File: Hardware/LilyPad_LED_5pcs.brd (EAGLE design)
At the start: 27.4 x 12.8 mm, 27 parts

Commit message: Updated Brd File
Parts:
- moved U$3 0.22 mm to (14.0, 6.61)
- moved U$5 0.20 mm to (25.1, 6.63)
- moved U$1 0.20 mm to (2.75, 6.62)
- moved U$4 0.20 mm to (19.5, 6.60)
- moved U$2 0.18 mm to (8.38, 6.61)

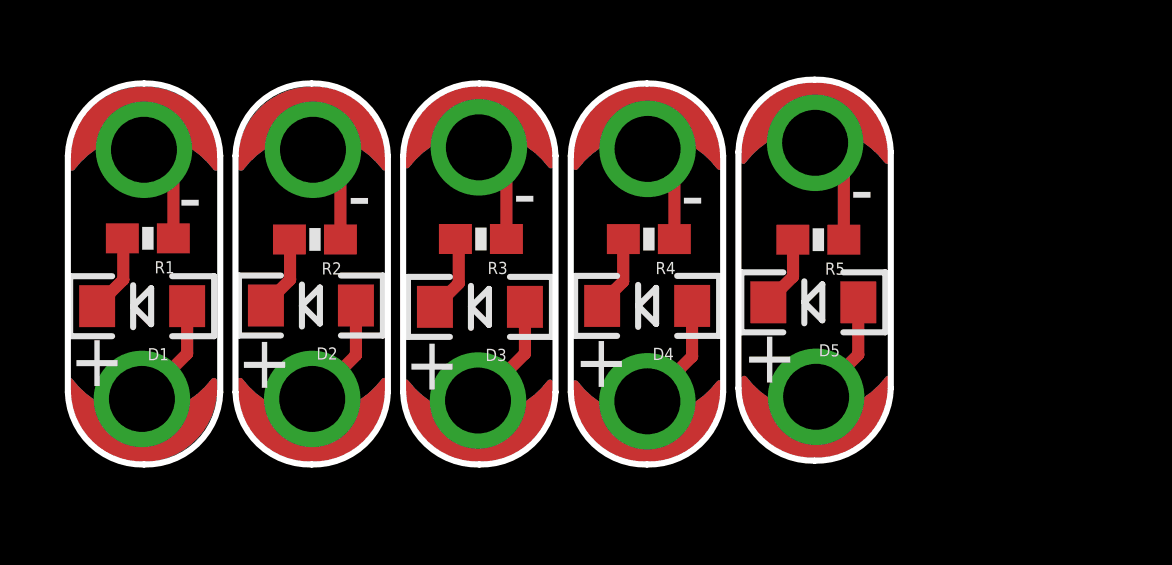
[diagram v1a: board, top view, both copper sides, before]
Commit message: Updated Brd files -- Chnaged orientation of LilyPad logo and cleaned up the centering a bit
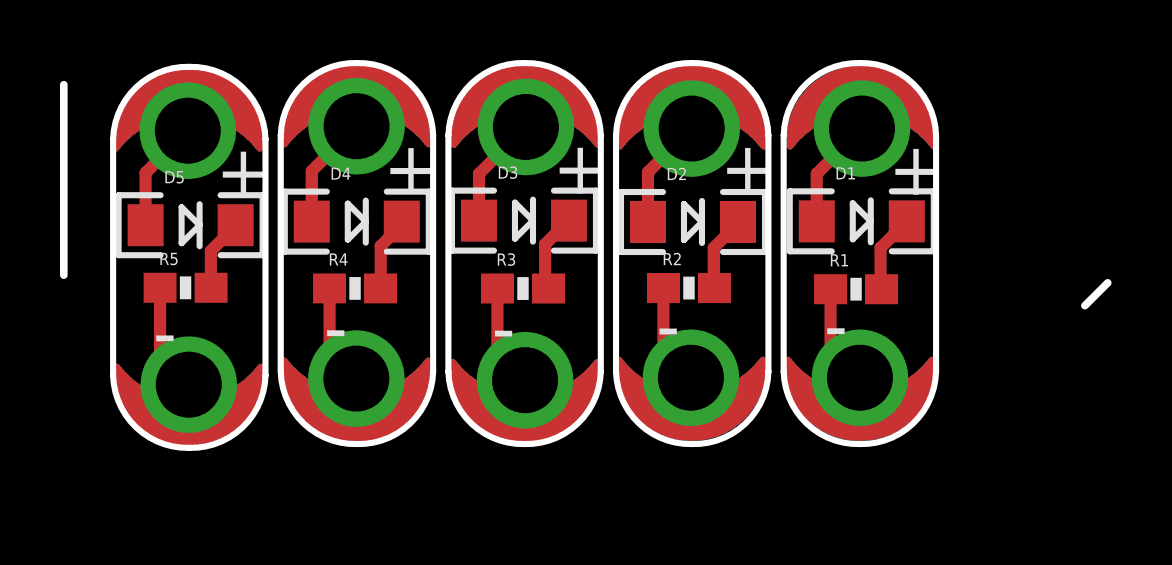
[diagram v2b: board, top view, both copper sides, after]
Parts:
- moved LED+1 25.6 mm to (26.6, 11.5), turned to 180 degrees
- moved LED-1 25.0 mm to (26.5, 3.19), turned to 0 degrees
- moved D1 24.2 mm to (26.6, 8.40), turned to 0 degrees
- moved U$1 23.9 mm to (26.6, 7.28)
- moved R1 23.7 mm to (26.4, 6.14), turned to 0 degrees
- moved LED+5 22.7 mm to (4.13, 11.4), turned to 180 degrees
- moved LED-5 22.4 mm to (4.17, 2.95), turned to 0 degrees
- moved R5 21.2 mm to (4.06, 6.18), turned to 0 degrees
- moved D5 20.9 mm to (4.23, 8.27), turned to 0 degrees
- moved U$5 20.8 mm to (4.36, 7.06)
- moved LED+2 15.5 mm to (20.9, 11.5), turned to 180 degrees
- moved LED-2 14.7 mm to (20.9, 3.19), turned to 0 degrees
- moved LED+4 13.3 mm to (9.76, 11.6), turned to 180 degrees
- moved D2 13.0 mm to (21.0, 8.38), turned to 0 degrees
- moved U$2 12.6 mm to (21.0, 7.27)
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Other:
- board size 27.4 x 12.8 mm -> 34.8 x 12.8 mm

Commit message: Updated board files
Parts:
- moved U$5 0.34 mm to (4.14, 7.32)
- moved U$4 0.29 mm to (9.72, 7.46)
- moved U$3 0.27 mm to (15.3, 7.44)
- moved R1 0.25 mm to (26.7, 6.14)
- moved U$1 0.20 mm to (26.6, 7.49)
- moved U$2 0.19 mm to (20.9, 7.44)
- moved R3 0.10 mm to (15.4, 6.16)
- moved R5 0.10 mm to (4.16, 6.18)
- moved R2 0.05 mm to (20.9, 6.17)
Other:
- board size 34.8 x 12.8 mm -> 34.8 x 14.6 mm
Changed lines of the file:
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@@
 <text x="26.1340625" y="5.847078125" size="1.778" layer="21" font="vector" ratio="15" rot="R180">-</text>
 <text x="20.54098125" y="5.836915625" size="1.778" layer="21" font="vector" ratio="15" rot="R180">-</text>
-<text x="15.05458125" y="5.7658" size="1.778" layer="21" font="vector" ratio="15" rot="R180">-</text>
+<text x="15.07998125" y="5.7404" size="1.778" layer="21" font="vector" ratio="15" rot="R180">-</text>
 <text x="9.4615" y="5.778496875" size="1.778" layer="21" font="vector" ratio="15" rot="R180">-</text>
 <text x="3.766821875" y="5.60831875" size="1.778" layer="21" font="vector" ratio="15" rot="R180">-</text>
@@
 <wire x1="0" y1="12.954" x2="0" y2="6.604" width="0.254" layer="20"/>
 <wire x1="34.036" y1="5.588" x2="34.798" y2="6.35" width="0.254" layer="20"/>
+<wire x1="4.1402" y1="0.5842" x2="4.2926" y2="0.4318" width="0.254" layer="20"/>
+<wire x1="20.9042" y1="-0.6858" x2="21.1328" y2="-0.9144" width="0.254" layer="20"/>
 </plain>
 <attributes>
@@
 <element name="LED-4" library="LilyPad-Wearables" package="PETAL-SMALL-2SIDE" value="SEWTAP6" x="9.751059375" y="3.15721875"/>
 <element name="LED-5" library="LilyPad-Wearables" package="PETAL-SMALL-2SIDE" value="SEWTAP6" x="4.165603125" y="2.95401875"/>
-<element name="R1" library="SparkFun-Resistors" package="0603-RES" value="150" x="26.408378125" y="6.1366375">
-<attribute name="PROD-ID" value="13326" x="26.408378125" y="6.1366375" size="1.778" layer="27" display="off"/>
-</element>
-<element name="R2" library="SparkFun-Resistors" package="0603-RES" value="150" x="20.8381625" y="6.174740625">
-<attribute name="PROD-ID" value="13326" x="20.8381625" y="6.174740625" size="1.778" layer="27" display="off"/>
-</element>
-<element name="R3" library="SparkFun-Resistors" package="0603-RES" value="150" x="15.306040625" y="6.159496875">
-<attribute name="PROD-ID" value="13326" x="15.306040625" y="6.159496875" size="1.778" layer="27" display="off"/>
+<element name="R1" library="SparkFun-Resistors" package="0603-RES" value="150" x="26.662378125" y="6.1366375">
+<attribute name="PROD-ID" value="13326" x="26.662378125" y="6.1366375" size="1.778" layer="27" display="off"/>
+</element>
+<element name="R2" library="SparkFun-Resistors" package="0603-RES" value="150" x="20.8889625" y="6.174740625">
+<attribute name="PROD-ID" value="13326" x="20.8889625" y="6.174740625" size="1.778" layer="27" display="off"/>
+</element>
+<element name="R3" library="SparkFun-Resistors" package="0603-RES" value="150" x="15.407640625" y="6.159496875">
+<attribute name="PROD-ID" value="13326" x="15.407640625" y="6.159496875" size="1.778" layer="27" display="off"/>
 </element>
 <element name="R4" library="SparkFun-Resistors" package="0603-RES" value="150" x="9.70788125" y="6.1620375">
 <attribute name="PROD-ID" value="13326" x="9.70788125" y="6.1620375" size="1.778" layer="27" display="off"/>
 </element>
-<element name="R5" library="SparkFun-Resistors" package="0603-RES" value="150" x="4.05891875" y="6.18235625">
-<attribute name="PROD-ID" value="13326" x="4.05891875" y="6.18235625" size="1.778" layer="27" display="off"/>
-</element>
-<element name="U$1" library="LilyPad-Wearables" package="LOGO-L" value="" x="26.629359375" y="7.28218125" rot="MR0"/>
-<element name="U$2" library="LilyPad-Wearables" package="LOGO-L" value="" x="20.980396875" y="7.266940625" rot="MR0"/>
-<element name="U$3" library="LilyPad-Wearables" package="LOGO-L" value="" x="15.476221875" y="7.266940625" rot="MR0"/>
-<element name="U$4" library="LilyPad-Wearables" package="LOGO-L" value="" x="9.895840625" y="7.23138125" rot="MR0"/>
-<element name="U$5" library="LilyPad-Wearables" package="LOGO-L" value="" x="4.36371875" y="7.063740625" rot="MR0"/>
+<element name="R5" library="SparkFun-Resistors" package="0603-RES" value="150" x="4.16051875" y="6.18235625">
+<attribute name="PROD-ID" value="13326" x="4.16051875" y="6.18235625" size="1.778" layer="27" display="off"/>
+</element>
+<element name="U$1" library="LilyPad-Wearables" package="LOGO-L" value="" x="26.629359375" y="7.48538125" rot="MR0"/>
+<element name="U$2" library="LilyPad-Wearables" package="LOGO-L" value="" x="20.904196875" y="7.444740625" rot="MR0"/>
+<element name="U$3" library="LilyPad-Wearables" package="LOGO-L" value="" x="15.273021875" y="7.444740625" rot="MR0"/>
+<element name="U$4" library="LilyPad-Wearables" package="LOGO-L" value="" x="9.718040625" y="7.45998125" rot="MR0"/>
+<element name="U$5" library="LilyPad-Wearables" package="LOGO-L" value="" x="4.13511875" y="7.317740625" rot="MR0"/>
 <element name="FRAME1" library="SparkFun-Aesthetics" package="CREATIVE_COMMONS" value="FRAME-LETTER" x="-5.542278125" y="-7.134859375"/>
 <element name="U$6" library="SparkFun-Aesthetics" package="REVISION" value="REVISION" x="5.66928125" y="-9.8552"/>
@@
 <contactref element="R1" pad="1"/>
 <contactref element="LED-1" pad="1"/>
-<wire x1="25.558378125" y1="6.1366375" x2="25.558378125" y2="4.164703125" width="0.4064" layer="1"/>
 <wire x1="25.558378125" y1="4.164703125" x2="26.537921875" y2="3.185159375" width="0.4064" layer="1"/>
+<wire x1="25.558378125" y1="4.164703125" x2="25.558378125" y2="5.8826375" width="0.4064" layer="1"/>
+<wire x1="25.558378125" y1="5.8826375" x2="25.812378125" y2="6.1366375" width="0.4064" layer="1"/>
 </signal>
 <signal name="1">
@@
 <wire x1="28.09888125" y1="8.399778125" x2="28.09888125" y2="8.388478125" width="0.4064" layer="1"/>
 <wire x1="28.09888125" y1="8.388478125" x2="27.2262625" y2="7.515859375" width="0.4064" layer="1"/>
-<wire x1="27.2262625" y1="7.515859375" x2="27.2262625" y2="6.168753125" width="0.4064" layer="1"/>
-<wire x1="27.2262625" y1="6.168753125" x2="27.258378125" y2="6.1366375" width="0.4064" layer="1"/>
+<wire x1="27.2262625" y1="7.515859375" x2="27.2262625" y2="6.422753125" width="0.4064" layer="1"/>
+<wire x1="27.2262625" y1="6.422753125" x2="27.512378125" y2="6.1366375" width="0.4064" layer="1"/>
 </signal>
 <signal name="4">
@@
 <wire x1="22.47278125" y1="8.322440625" x2="21.6662" y2="7.515859375" width="0.4064" layer="1"/>
 <wire x1="21.6662" y1="7.515859375" x2="21.6662" y2="6.196703125" width="0.4064" layer="1"/>
-<wire x1="21.6662" y1="6.196703125" x2="21.6881625" y2="6.174740625" width="0.4064" layer="1"/>
+<wire x1="21.6662" y1="6.196703125" x2="21.7389625" y2="6.174740625" width="0.4064" layer="1"/>
 </signal>
 <signal name="6">
 <contactref element="R2" pad="1"/>
 <contactref element="LED-2" pad="1"/>
-<wire x1="19.9881625" y1="6.174740625" x2="19.9881625" y2="4.101196875" width="0.4064" layer="1"/>
 <wire x1="19.9881625" y1="4.101196875" x2="20.9042" y2="3.185159375" width="0.4064" layer="1"/>
+<wire x1="19.9881625" y1="4.101196875" x2="19.9881625" y2="6.123940625" width="0.4064" layer="1"/>
+<wire x1="19.9881625" y1="6.123940625" x2="20.0389625" y2="6.174740625" width="0.4064" layer="1"/>
 </signal>
 <signal name="7">
@@
 <wire x1="16.8390625" y1="8.422640625" x2="16.83004375" y2="8.422640625" width="0.4064" layer="1"/>
 <wire x1="16.83004375" y1="8.422640625" x2="16.04518125" y2="7.637778125" width="0.4064" layer="1"/>
-<wire x1="16.04518125" y1="7.637778125" x2="16.04518125" y2="6.27035625" width="0.4064" layer="1"/>
-<wire x1="16.04518125" y1="6.27035625" x2="16.156040625" y2="6.159496875" width="0.4064" layer="1"/>
+<wire x1="16.04518125" y1="6.27035625" x2="16.257640625" y2="6.159496875" width="0.4064" layer="1"/>
+<wire x1="16.04518125" y1="7.637778125" x2="16.04518125" y2="6.37195625" width="0.4064" layer="1"/>
+<wire x1="16.04518125" y1="6.37195625" x2="16.257640625" y2="6.159496875" width="0.4064" layer="1"/>
 </signal>
 <signal name="9">
 <contactref element="R3" pad="1"/>
 <contactref element="LED-3" pad="1"/>
-<wire x1="14.456040625" y1="6.159496875" x2="14.456040625" y2="4.022459375" width="0.4064" layer="1"/>
 <wire x1="14.456040625" y1="4.022459375" x2="15.374621875" y2="3.103878125" width="0.4064" layer="1"/>
+<wire x1="14.456040625" y1="4.022459375" x2="14.456040625" y2="6.057896875" width="0.4064" layer="1"/>
+<wire x1="14.456040625" y1="6.057896875" x2="14.557640625" y2="6.159496875" width="0.254" layer="1"/>
 </signal>
 <signal name="12">
@@
 <wire x1="5.7265625" y1="8.238621875" x2="4.9022" y2="7.414259375" width="0.4064" layer="1"/>
 <wire x1="4.9022" y1="7.414259375" x2="4.9022" y2="6.189075" width="0.4064" layer="1"/>
-<wire x1="4.9022" y1="6.189075" x2="4.90891875" y2="6.18235625" width="0.4064" layer="1"/>
+<wire x1="4.9022" y1="6.189075" x2="5.01051875" y2="6.18235625" width="0.4064" layer="1"/>
 </signal>
 <signal name="15">
 <contactref element="R5" pad="1"/>
 <contactref element="LED-5" pad="1"/>
-<wire x1="3.20891875" y1="6.18235625" x2="3.20891875" y2="3.910703125" width="0.4064" layer="1"/>
 <wire x1="3.20891875" y1="3.910703125" x2="4.165603125" y2="2.95401875" width="0.4064" layer="1"/>
+<wire x1="3.20891875" y1="3.910703125" x2="3.20891875" y2="6.08075625" width="0.254" layer="1"/>
+<wire x1="3.20891875" y1="6.08075625" x2="3.31051875" y2="6.18235625" width="0.254" layer="1"/>
 </signal>
 </signals>

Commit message: Updated Brd File per Eng Design Rev
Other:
- board size 34.8 x 14.6 mm -> 27.4 x 12.8 mm
- board text added: "Purple Solder Mask"
- board text added: "v11"
- board text removed: "Purple Silk"
